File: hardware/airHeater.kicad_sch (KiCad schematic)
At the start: 9 parts, among them Q6 60T03H, Q7 BTA16-600B, U1 MOC3063M

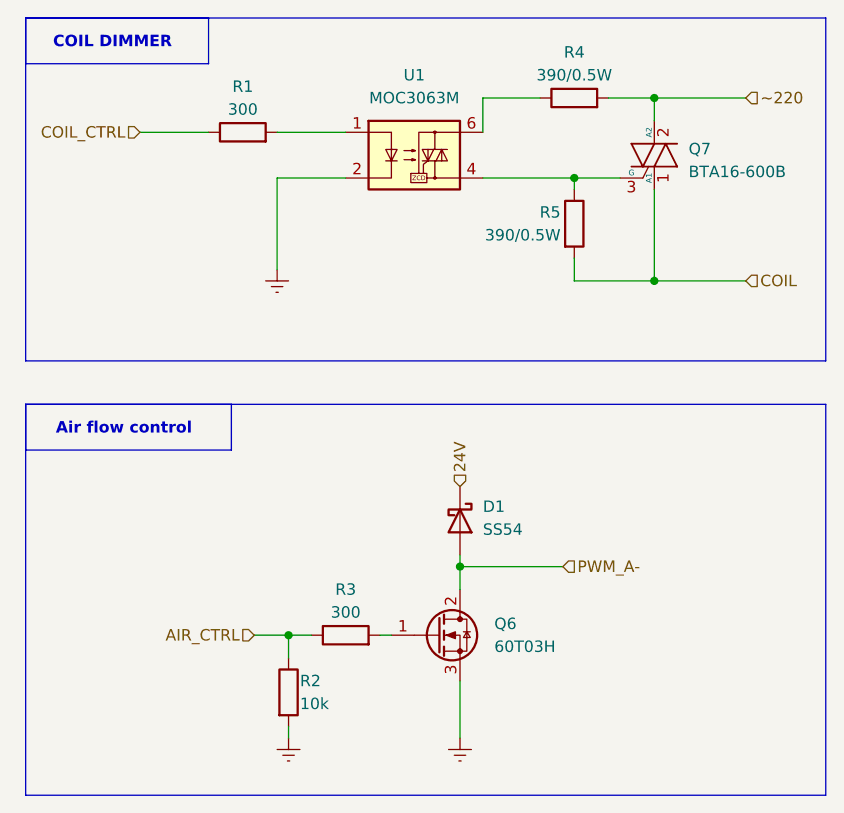
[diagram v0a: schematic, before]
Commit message: mvp
features:
	Logic Power Supply
	Safety Relay
	Main Unit
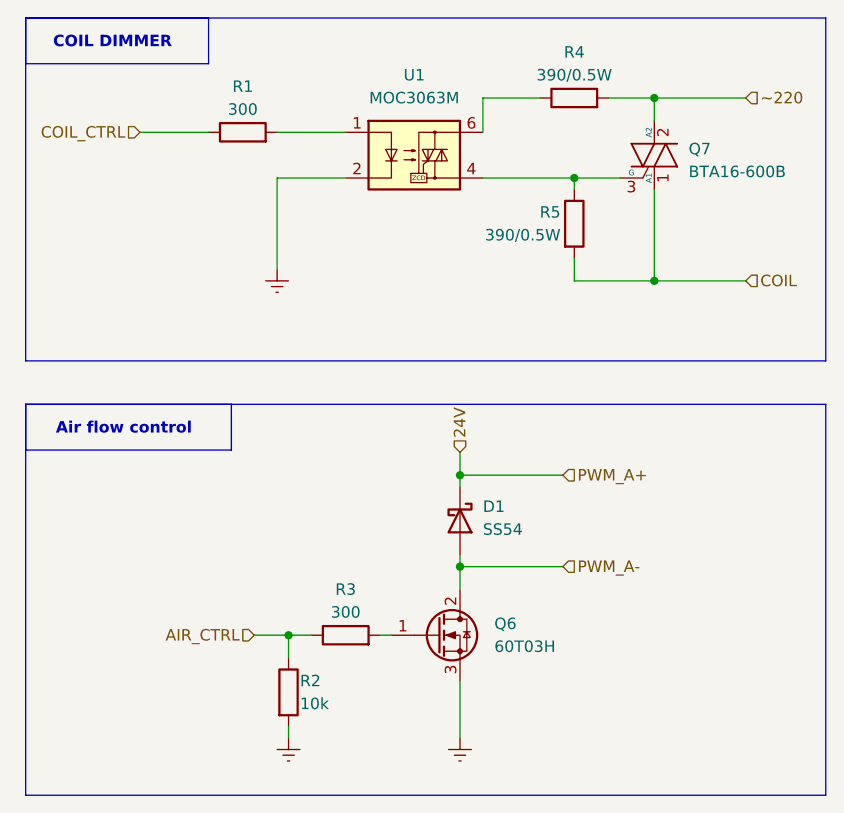
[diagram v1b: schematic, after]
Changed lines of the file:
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@@
+	)
+	(junction
+		(at 109.22 76.2)
+		(diameter 0)
+		(color 0 0 0 0)
 	)
 	(junction
@@
 	(wire
 		(pts
+			(xy 109.22 73.66) (xy 109.22 76.2)
+		)
+		(stroke
+			(width 0)
+			(type default)
+		)
+	)
+	(wire
+		(pts
 			(xy 109.22 86.36) (xy 120.65 86.36)
 		)
@@
 	(wire
 		(pts
+			(xy 109.22 76.2) (xy 109.22 77.47)
+		)
+		(stroke
+			(width 0)
+			(type default)
+		)
+	)
+	(wire
+		(pts
 			(xy 109.22 99.06) (xy 109.22 105.41)
 		)
@@
 		(pts
 			(xy 111.76 43.18) (xy 121.92 43.18)
+		)
+		(stroke
+			(width 0)
+			(type default)
+		)
+	)
+	(wire
+		(pts
+			(xy 109.22 76.2) (xy 120.65 76.2)
 		)
 		(stroke
@@
 		)
 	)
+	(hierarchical_label "PWM_A+"
+		(shape input)
+		(at 120.65 76.2 0)
+		(effects
+			(font
+				(size 1.27 1.27)
+			)
+			(justify left)
+		)
+	)
 	(hierarchical_label "24V"
 		(shape input)
-		(at 109.22 77.47 90)
-		(effects
-			(font
+		(at 109.22 73.66 90)
+		(effects
+			(font

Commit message: starting pcb
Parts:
- D1: footprint Diode_THT:D_DO-35_SOD27_P2.54mm_Vertical_KathodeUp -> Diode_SMD:D_SMA
- Q6: footprint (none) -> Package_TO_SOT_SMD:TO-252-2
- R1, R2, R3: footprint (none) -> Resistor_SMD:R_0603_1608Metric
- R4, R5: footprint (none) -> Resistor_THT:R_Axial_DIN0309_L9.0mm_D3.2mm_P12.70mm_Horizontal
- U1: footprint (none) -> Package_DIP:DIP-6_W7.62mm_LongPads
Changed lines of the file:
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@@
 			)
 		)
-		(property "Footprint" ""
+		(property "Footprint" "Resistor_THT:R_Axial_DIN0309_L9.0mm_D3.2mm_P12.70mm_Horizontal"
 			(at 120.142 48.26 90)
 			(effects
@@
 			)
 		)
-		(property "Footprint" ""
+		(property "Footprint" "Package_TO_SOT_SMD:TO-252-2"
 			(at 111.76 91.44 0)
 			(effects
@@
 			)
 		)
-		(property "Footprint" ""
+		(property "Footprint" "Resistor_SMD:R_0603_1608Metric"
 			(at 85.09 39.878 90)
 			(effects
@@
 			)
 		)
-		(property "Footprint" "Diode_THT:D_DO-35_SOD27_P2.54mm_Vertical_KathodeUp"
+		(property "Footprint" "Diode_SMD:D_SMA"
 			(at 104.775 81.28 0)
 			(effects
@@
 			)
 		)
-		(property "Footprint" ""
+		(property "Footprint" "Package_DIP:DIP-6_W7.62mm_LongPads"
 			(at 99.06 45.72 0)
 			(effects
@@
 			)
 		)
-		(property "Footprint" ""
+		(property "Footprint" "Resistor_SMD:R_0603_1608Metric"
 			(at 96.52 95.758 90)
 			(effects
@@
 			)
 		)
-		(property "Footprint" ""
+		(property "Footprint" "Resistor_SMD:R_0603_1608Metric"
 			(at 88.392 100.33 90)
 			(effects
@@
 			)
 		)
-		(property "Footprint" ""
+		(property "Footprint" "Resistor_THT:R_Axial_DIN0309_L9.0mm_D3.2mm_P12.70mm_Horizontal"
 			(at 121.92 36.068 90)
 			(effects

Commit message: pcb mvp
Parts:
- Q6: value 60T03H -> AO3400A; footprint Package_TO_SOT_SMD:TO-252-2 -> Package_TO_SOT_SMD:SOT-23

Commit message: last
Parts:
- removed Q6: AO3400A, Package_TO_SOT_SMD:SOT-23, symbol SolderingStationLib:60T03H
- added Q4: IRLZ44N, Package_TO_SOT_THT:TO-220-3_Vertical, symbol Transistor_FET:Q_NMOS_GDS
- D1: LCSC (none) -> C22452
- R1, R3: footprint Resistor_SMD:R_0603_1608Metric -> Resistor_SMD:R_0805_2012Metric_Pad1.20x1.40mm_HandSolder; LCSC (none) -> C23025
- R2: footprint Resistor_SMD:R_0603_1608Metric -> Resistor_SMD:R_0805_2012Metric_Pad1.20x1.40mm_HandSolder; LCSC (none) -> C25804
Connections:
- net GNDREF: now also Q4.3 (S)
- net PWM_A-: now also Q4.2 (D)
- net at R3.2: now also Q4.1 (G)
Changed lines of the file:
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@@
+			)
+		)
+		(property "LCSC" ""
+			(at 121.92 48.26 0)
+			(hide yes)
+			(show_name no)
+			(do_not_autoplace no)
+			(effects
+				(font
+					(size 1.27 1.27)
+				)
 			)
 		)
@@
 			)
 		)
+		(property "LCSC" ""
+			(at 130.81 40.64 0)
+			(hide yes)
+			(show_name no)
+			(do_not_autoplace no)
+			(effects
+				(font
+					(size 1.27 1.27)
+				)
+			)
+		)
 		(pin "1"
 		)
@@
 				(path "/23f2f192-8d8a-4d18-9a9e-f5d6a1224b2d/521a69e4-8121-48bb-87b1-847743f69fdd"
 					(reference "Q7")
-					(unit 1)
-				)
-			)
-		)
-	)
-	(symbol
-		(lib_id "SolderingStationLib:60T03H")
-		(at 106.68 93.98 0)
-		(unit 1)
-		(body_style 1)
-		(exclude_from_sim no)
-		(in_bom yes)
-		(on_board yes)
-		(in_pos_files yes)
-		(dnp no)
-		(fields_autoplaced yes)
-		(property "Reference" "Q6"
-			(at 113.03 92.7099 0)
-			(show_name no)
-			(do_not_autoplace no)
-			(effects
-				(font
-					(size 1.27 1.27)
-				)
-				(justify left)
-			)
-		)
-		(property "Value" "AO3400A"
-			(at 113.03 95.2499 0)
-			(show_name no)
-			(do_not_autoplace no)
-			(effects
-				(font
-					(size 1.27 1.27)
-				)
-				(justify left)
-			)
-		)
-		(property "Footprint" "Package_TO_SOT_SMD:SOT-23"
-			(at 111.76 91.44 0)
-			(hide yes)
-			(show_name no)
-			(do_not_autoplace no)
-			(effects
-				(font
-					(size 1.27 1.27)
-				)
-			)
-		)
-		(property "Datasheet" ""
-			(at 106.68 93.98 0)
-			(hide yes)
-			(show_name no)
-			(do_not_autoplace no)
-			(effects
-				(font
-					(size 1.27 1.27)
-				)
-			)
-		)
-		(property "Description" "N-MOSFET transistor, gate/drain/source"
-			(at 106.68 93.98 0)
-			(hide yes)
-			(show_name no)
-			(do_not_autoplace no)
-			(effects
-				(font
-					(size 1.27 1.27)
-				)
-			)
-		)
-		(pin "3"
-		)
-		(pin "1"
-		)
-		(pin "2"
-		)
-		(instances
-			(project "SolderingStation"
-				(path "/23f2f192-8d8a-4d18-9a9e-f5d6a1224b2d/521a69e4-8121-48bb-87b1-847743f69fdd"
-					(reference "Q6")
 					(unit 1)
 				)
@@
 			)
 		)
-		(property "Footprint" "Resistor_SMD:R_0603_1608Metric"
+		(property "Footprint" "Resistor_SMD:R_0805_2012Metric_Pad1.20x1.40mm_HandSolder"
 			(at 85.09 39.878 90)
 			(hide yes)
@@
 		(property "Description" "Resistor"
 			(at 85.09 38.1 0)
+			(hide yes)
+			(show_name no)
+			(do_not_autoplace no)
+			(effects
+				(font
+					(size 1.27 1.27)
+				)
+			)
+		)
+		(property "LCSC" "C23025"
+			(at 85.09 38.1 90)
 			(hide yes)
 			(show_name no)
@@
 			)
 		)
+		(property "LCSC" "C22452"
+			(at 109.22 81.28 90)
+			(hide yes)
+			(show_name no)
+			(do_not_autoplace no)
+			(effects
+				(font
+					(size 1.27 1.27)
+				)
+			)
+		)
 		(pin "1"
 		)
@@
 			)
 		)
+		(property "LCSC" ""
+			(at 104.14 40.64 0)
+			(hide yes)
+			(show_name no)
+			(do_not_autoplace no)
+			(effects
+				(font
+					(size 1.27 1.27)
+				)
+			)
+		)
 		(pin "1"
 		)
@@
 			)
 		)
-		(property "Footprint" "Resistor_SMD:R_0603_1608Metric"
+		(property "Footprint" "Resistor_SMD:R_0805_2012Metric_Pad1.20x1.40mm_HandSolder"
 			(at 96.52 95.758 90)
 			(hide yes)
@@
 			)
 		)
+		(property "LCSC" "C23025"
+			(at 96.52 93.98 90)
+			(hide yes)
+			(show_name no)
+			(do_not_autoplace no)
+			(effects
+				(font
+					(size 1.27 1.27)
+				)
+			)
+		)
 		(pin "2"
 		)
@@
 			)
 		)
-		(property "Footprint" "Resistor_SMD:R_0603_1608Metric"
+		(property "Footprint" "Resistor_SMD:R_0805_2012Metric_Pad1.20x1.40mm_HandSolder"
 			(at 88.392 100.33 90)
 			(hide yes)
@@
 			)
 		)
+		(property "LCSC" "C25804"
+			(at 90.17 100.33 0)
+			(hide yes)
+			(show_name no)
+			(do_not_autoplace no)
+			(effects
+				(font
+					(size 1.27 1.27)
+				)
+			)
+		)
 		(pin "2"
 		)
@@
 				(path "/23f2f192-8d8a-4d18-9a9e-f5d6a1224b2d/521a69e4-8121-48bb-87b1-847743f69fdd"
 					(reference "R2")
+					(unit 1)
+				)
+			)
+		)
+	)
+	(symbol
+		(lib_id "Transistor_FET:Q_NMOS_GDS")
+		(at 106.68 93.98 0)
+		(unit 1)
+		(body_style 1)
+		(exclude_from_sim no)
+		(in_bom yes)
+		(on_board yes)
+		(in_pos_files yes)
+		(dnp no)
+		(fields_autoplaced yes)
+		(property "Reference" "Q4"
+			(at 113.03 92.7099 0)
+			(show_name no)
+			(do_not_autoplace no)
+			(effects
+				(font
+					(size 1.27 1.27)
+				)
+				(justify left)
+			)
+		)
+		(property "Value" "IRLZ44N"
+			(at 113.03 95.2499 0)
+			(show_name no)
+			(do_not_autoplace no)
+			(effects
+				(font
+					(size 1.27 1.27)
+				)
+				(justify left)
+			)
+		)
+		(property "Footprint" "Package_TO_SOT_THT:TO-220-3_Vertical"
+			(at 111.76 91.44 0)
+			(hide yes)
+			(show_name no)
+			(do_not_autoplace no)
+			(effects
+				(font
+					(size 1.27 1.27)
+				)
+			)
+		)
+		(property "Datasheet" ""
+			(at 106.68 93.98 0)
+			(hide yes)
+			(show_name no)
+			(do_not_autoplace no)
+			(effects
+				(font
+					(size 1.27 1.27)
+				)
+			)
+		)
+		(property "Description" "N-MOSFET transistor, gate/drain/source"
+			(at 106.68 93.98 0)
+			(hide yes)
+			(show_name no)
+			(do_not_autoplace no)
+			(effects
+				(font
+					(size 1.27 1.27)
+				)
+			)
+		)
+		(property "LCSC" ""
+			(at 106.68 93.98 0)
+			(hide yes)
+			(show_name no)
+			(do_not_autoplace no)
+			(effects
+				(font
+					(size 1.27 1.27)
+				)
+			)
+		)
+		(pin "3"
+		)
+		(pin "1"
+		)
+		(pin "2"
+		)
+		(instances
+			(project "SolderingStation"
+				(path "/23f2f192-8d8a-4d18-9a9e-f5d6a1224b2d/521a69e4-8121-48bb-87b1-847743f69fdd"
+					(reference "Q4")
 					(unit 1)
 				)
@@
 			(hide yes)
 			(show_name no)
+			(do_not_autoplace no)
+			(effects
+				(font
+					(size 1.27 1.27)
+				)
+			)
+		)
+		(property "LCSC" ""
+			(at 121.92 34.29 90)
+			(hide yes)
+			(show_name no)
